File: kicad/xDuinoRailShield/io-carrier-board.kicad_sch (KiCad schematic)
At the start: 6 parts, among them J5 Screw_Terminal_01x02

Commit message: More options, more Partnumbers
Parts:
- J5: LCSC (none) -> C8269
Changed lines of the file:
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@@
         )
         (path "/e63e39d7-6ac0-4ffd-8aa3-1841a4541b55/73623b68-3f11-49c2-b33b-f7aef9e34c5f"
-          (reference "#PWR01") (unit 1)
+          (reference "#PWR0501") (unit 1)
         )
       )
@@
         )
         (path "/e63e39d7-6ac0-4ffd-8aa3-1841a4541b55/73623b68-3f11-49c2-b33b-f7aef9e34c5f"
-          (reference "D1") (unit 1)
+          (reference "D501") (unit 1)
         )
       )
@@
         )
         (path "/e63e39d7-6ac0-4ffd-8aa3-1841a4541b55/73623b68-3f11-49c2-b33b-f7aef9e34c5f"
-          (reference "R1") (unit 1)
+          (reference "R501") (unit 1)
         )
       )
@@
         )
         (path "/e63e39d7-6ac0-4ffd-8aa3-1841a4541b55/73623b68-3f11-49c2-b33b-f7aef9e34c5f"
-          (reference "A1") (unit 1)
+          (reference "A501") (unit 1)
         )
       )
@@
         )
         (path "/e63e39d7-6ac0-4ffd-8aa3-1841a4541b55/73623b68-3f11-49c2-b33b-f7aef9e34c5f"
-          (reference "#PWR09") (unit 1)
+          (reference "#PWR0504") (unit 1)
         )
       )
@@
         )
         (path "/e63e39d7-6ac0-4ffd-8aa3-1841a4541b55/73623b68-3f11-49c2-b33b-f7aef9e34c5f"
-          (reference "R2") (unit 1)
+          (reference "R502") (unit 1)
         )
       )
@@
         )
         (path "/e63e39d7-6ac0-4ffd-8aa3-1841a4541b55/73623b68-3f11-49c2-b33b-f7aef9e34c5f"
+          (reference "#PWR0502") (unit 1)
+        )
+      )
+    )
+  )
+  (symbol (lib_id "Connector:Screw_Terminal_01x02") (at 72.39 59.69 180) (unit 1)
+    (in_bom yes) (on_board yes) (dnp no)
+    (property "Reference" "J5" (at 72.39 62.23 0)
+      (effects (font (size 1.27 1.27)) (justify left))
+    )
+    (property "Value" "Screw_Terminal_01x02" (at 91.44 64.77 0)
+      (effects (font (size 1.27 1.27)) (justify left))
+    )
+    (property "Footprint" "TerminalBlock_4Ucon:TerminalBlock_4Ucon_1x02_P3.50mm_Vertical" (at 72.39 59.69 0)
+      (effects (font (size 1.27 1.27)) hide)
+    )
+    (property "Datasheet" "~" (at 72.39 59.69 0)
+      (effects (font (size 1.27 1.27)) hide)
+    )
+    (property "LCSC" "C8269" (at 72.39 59.69 0)
+      (effects (font (size 1.27 1.27)) hide)
+    )
+    (pin "1")
+    (pin "2")
+    (instances
+      (project "xDuinoRailShield"
+        (path "/e63e39d7-6ac0-4ffd-8aa3-1841a4541b55"
+          (reference "J5") (unit 1)
+        )
+        (path "/e63e39d7-6ac0-4ffd-8aa3-1841a4541b55/73623b68-3f11-49c2-b33b-f7aef9e34c5f"
+          (reference "J501") (unit 1)
+        )
+      )
+    )
+  )
+  (symbol (lib_id "power:+3V3") (at 212.09 52.07 0) (mirror y) (unit 1)
+    (in_bom yes) (on_board yes) (dnp no)
+    (property "Reference" "#PWR03" (at 212.09 55.88 0)
+      (effects (font (size 1.27 1.27)) hide)
+    )
+    (property "Value" "+3.3V" (at 211.709 49.022 90)
+      (effects (font (size 1.27 1.27)) (justify left))
+    )
+    (property "Footprint" "" (at 212.09 52.07 0)
+      (effects (font (size 1.27 1.27)))
+    )
+    (property "Datasheet" "" (at 212.09 52.07 0)
+      (effects (font (size 1.27 1.27)))
+    )
+    (pin "1")
+    (instances
+      (project "xDuinoRailShield"
+        (path "/e63e39d7-6ac0-4ffd-8aa3-1841a4541b55"
           (reference "#PWR03") (unit 1)
         )
-      )
-    )
-  )
-  (symbol (lib_id "Connector:Screw_Terminal_01x02") (at 72.39 59.69 180) (unit 1)
-    (in_bom yes) (on_board yes) (dnp no)
-    (property "Reference" "J5" (at 72.39 62.23 0)
-      (effects (font (size 1.27 1.27)) (justify left))
-    )
-    (property "Value" "Screw_Terminal_01x02" (at 91.44 64.77 0)
-      (effects (font (size 1.27 1.27)) (justify left))
-    )
-    (property "Footprint" "TerminalBlock_4Ucon:TerminalBlock_4Ucon_1x02_P3.50mm_Vertical" (at 72.39 59.69 0)
-      (effects (font (size 1.27 1.27)) hide)
-    )
-    (property "Datasheet" "~" (at 72.39 59.69 0)
-      (effects (font (size 1.27 1.27)) hide)
-    )
-    (property "LCSC" "" (at 72.39 59.69 0)
-      (effects (font (size 1.27 1.27)) hide)
-    )
-    (pin "1")
-    (pin "2")
-    (instances
-      (project "xDuinoRailShield"
-        (path "/e63e39d7-6ac0-4ffd-8aa3-1841a4541b55"
-          (reference "J5") (unit 1)
-        )
-        (path "/e63e39d7-6ac0-4ffd-8aa3-1841a4541b55/73623b68-3f11-49c2-b33b-f7aef9e34c5f"
-          (reference "J1") (unit 1)
-        )
-      )
-    )
-  )
-  (symbol (lib_id "power:+3V3") (at 212.09 52.07 0) (mirror y) (unit 1)
-    (in_bom yes) (on_board yes) (dnp no)
-    (property "Reference" "#PWR03" (at 212.09 55.88 0)
-      (effects (font (size 1.27 1.27)) hide)
-    )
-    (property "Value" "+3.3V" (at 211.709 49.022 90)
-      (effects (font (size 1.27 1.27)) (justify left))
-    )
-    (property "Footprint" "" (at 212.09 52.07 0)
-      (effects (font (size 1.27 1.27)))
-    )
-    (property "Datasheet" "" (at 212.09 52.07 0)
-      (effects (font (size 1.27 1.27)))
-    )
-    (pin "1")
-    (instances
-      (project "xDuinoRailShield"
-        (path "/e63e39d7-6ac0-4ffd-8aa3-1841a4541b55"
-          (reference "#PWR03") (unit 1)
-        )
-        (path "/e63e39d7-6ac0-4ffd-8aa3-1841a4541b55/73623b68-3f11-49c2-b33b-f7aef9e34c5f"
-          (reference "#PWR08") (unit 1)
+        (path "/e63e39d7-6ac0-4ffd-8aa3-1841a4541b55/73623b68-3f11-49c2-b33b-f7aef9e34c5f"
+          (reference "#PWR0503") (unit 1)
         )
       )
@@
         )
         (path "/e63e39d7-6ac0-4ffd-8aa3-1841a4541b55/73623b68-3f11-49c2-b33b-f7aef9e34c5f"
-          (reference "D3") (unit 1)
-        )
-      )
+          (reference "D502") (unit 1)
+        )
+      )

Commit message: Another iteration on the layout
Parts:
- J501: renamed from J5; footprint TerminalBlock_4Ucon:TerminalBlock_4Ucon_1x02_P3.50mm_Vertical -> TerminalBlock:TerminalBlock_bornier-2_P5.08mm
- renumbered A1 to A501, D1 to D501, D3 to D502, R1 to R501, R2 to R502

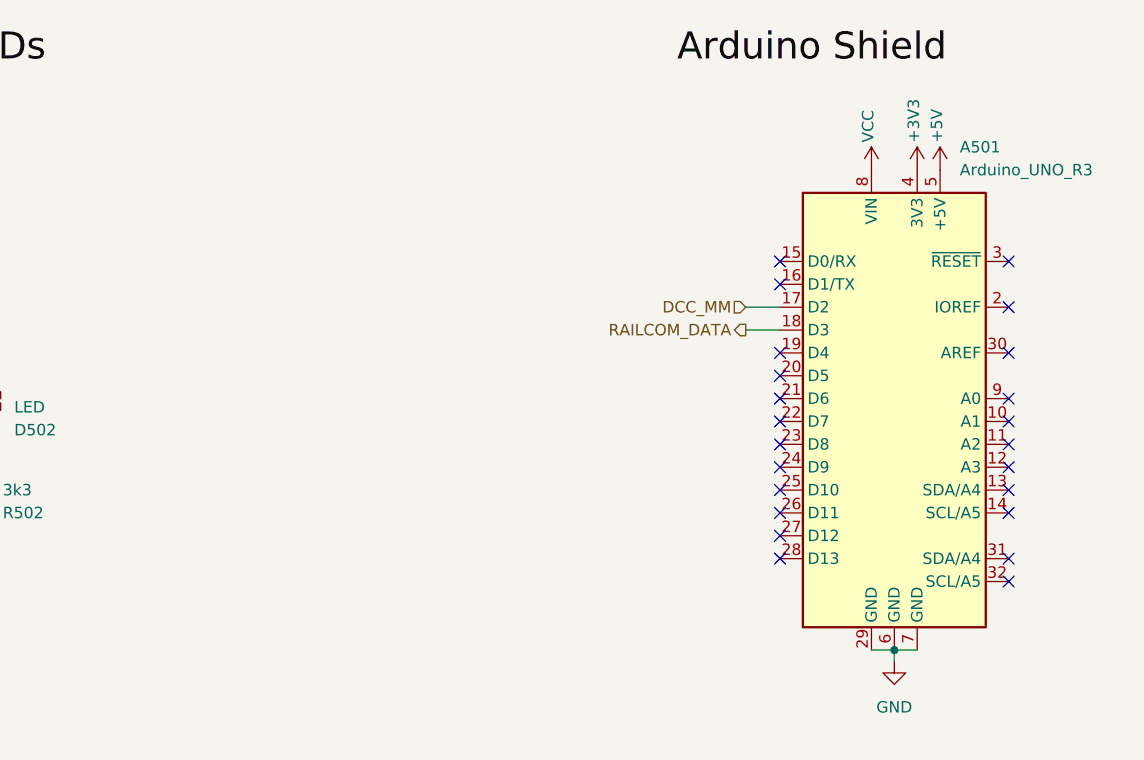
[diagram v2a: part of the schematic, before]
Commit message: Power Rails added to Arduino IO board
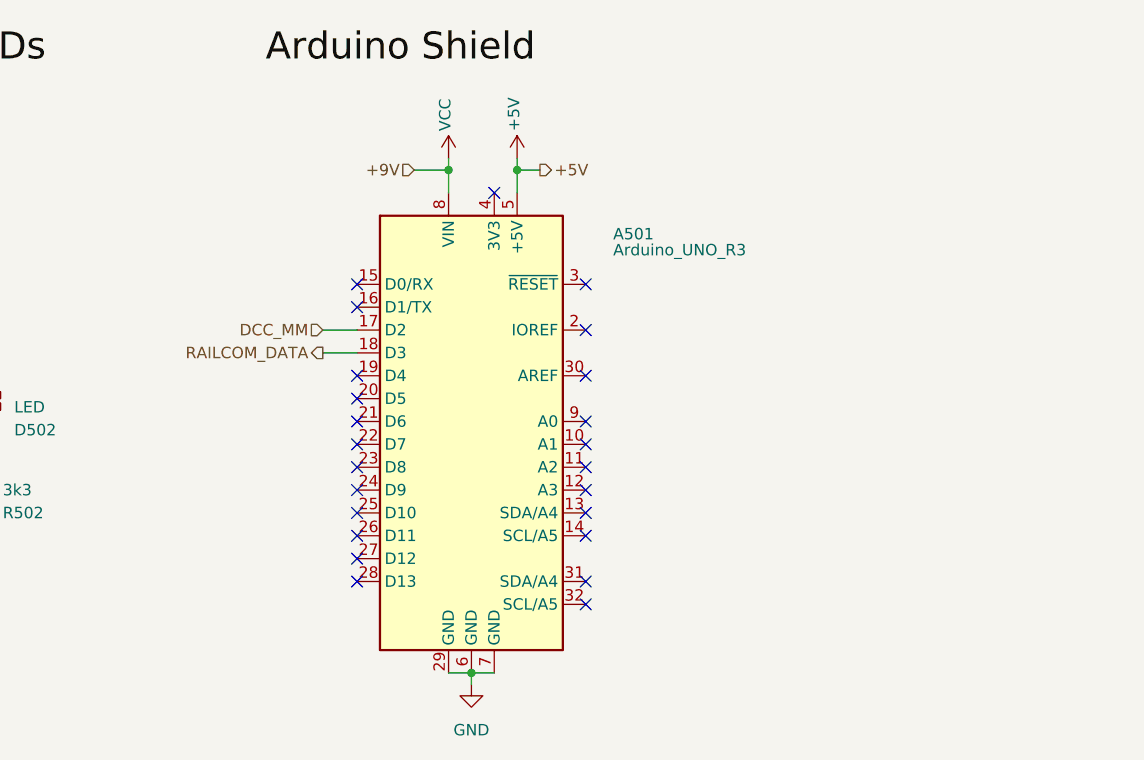
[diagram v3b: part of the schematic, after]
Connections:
- net +3V3: no longer names the net of A501.4 (3V3)
- no-connect marks 23 -> 24
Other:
- moved on the sheet: A501

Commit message: Add Analog signal extraction draft
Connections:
- net ANALOG_5V: now reaches A501.12 (A3)
- no-connect marks 24 -> 23
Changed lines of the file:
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@@
+	)
+	(junction
+		(at 162.56 110.49)
+		(diameter 0)
+		(color 0 0 0 0)
 	)
 	(junction
@@
 	)
 	(no_connect
-		(at 175.26 87.63)
-	)
-	(no_connect
 		(at 175.26 69.85)
 	)
@@
 	(wire
 		(pts
+			(xy 167.64 110.49) (xy 162.56 110.49)
+		)
+		(stroke
+			(width 0)
+			(type default)
+		)
+	)
+	(wire
+		(pts
 			(xy 160.02 50.8) (xy 160.02 52.07)
 		)
@@
 	(wire
 		(pts
-			(xy 162.56 109.22) (xy 162.56 107.95)
+			(xy 162.56 110.49) (xy 162.56 107.95)
+		)
+		(stroke
+			(width 0)
+			(type default)
+		)
+	)
+	(wire
+		(pts
+			(xy 162.56 111.76) (xy 162.56 110.49)
 		)
 		(stroke
@@
 		(pts
 			(xy 160.02 107.95) (xy 162.56 107.95)
+		)
+		(stroke
+			(width 0)
+			(type default)
+		)
+	)
+	(wire
+		(pts
+			(xy 175.26 87.63) (xy 184.15 87.63)
 		)
 		(stroke
@@
 		)
 	)
+	(hierarchical_label "GND"
+		(shape bidirectional)
+		(at 167.64 110.49 0)
+		(fields_autoplaced yes)
+		(effects
+			(font
+				(size 1.27 1.27)
+			)
+			(justify left)
+		)
+	)
 	(hierarchical_label "DCC_MM"
 		(shape input)
@@
 			)
 			(justify right)
+		)
+	)
+	(hierarchical_label "ANALOG_5V"
+		(shape input)
+		(at 184.15 87.63 0)
+		(fields_autoplaced yes)
+		(effects
+			(font
+				(size 1.27 1.27)
+			)
+			(justify left)
 		)
 	)
@@
 	(symbol
 		(lib_id "power:GND")
-		(at 162.56 109.22 0)
+		(at 162.56 111.76 0)
 		(unit 1)
 		(exclude_from_sim no)
@@
 		(fields_autoplaced yes)
 		(property "Reference" "#PWR05"
-			(at 162.56 115.57 0)
+			(at 162.56 118.11 0)
 			(effects
 				(font
@@
 		)
 		(property "Value" "GND"
-			(at 162.56 114.3 0)
+			(at 162.56 116.84 0)
 			(effects
 				(font
@@
 		)
 		(property "Footprint" ""
-			(at 162.56 109.22 0)
+			(at 162.56 111.76 0)
 			(effects
 				(font
@@
 		)
 		(property "Datasheet" ""
-			(at 162.56 109.22 0)
+			(at 162.56 111.76 0)
 			(effects
 				(font
@@
 		)
 		(property "Description" ""
-			(at 162.56 109.22 0)
-			(effects
-				(font
+			(at 162.56 111.76 0)
+			(effects
+				(font

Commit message: xXiaoCentralMini
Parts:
- added JP1: DAC_OUTPUT_SELECT, Jumper:SolderJumper-3_P1.3mm_Bridged12_RoundedPad1.0x1.5mm, symbol Jumper:SolderJumper_3_Bridged12
- added U7: MOUDLE-SEEEDUINO-XIAO-ESP32C3, MOUDLE14P-SMD-2.54-21X17.8MM, symbol MOUDLE-SEEEDUINO-XIAO-ESP32C3:MOUDLE-SEEEDUINO-XIAO-ESP32C3
- A1: renamed from A501; footprint Olis_Footprints:Arduino_UNO_R3_Double_Rows -> Module:Arduino_UNO_R3
- D8: renamed from D501; now not fitted
- D9: renamed from D502; now not fitted
- R12: renamed from R501; footprint Resistor_SMD:R_0805_2012Metric_Pad1.20x1.40mm_HandSolder -> Resistor_SMD:R_0603_1608Metric_Pad0.98x0.95mm_HandSolder; now not fitted
- R13: renamed from R502; footprint Resistor_SMD:R_0805_2012Metric_Pad1.20x1.40mm_HandSolder -> Resistor_SMD:R_0603_1608Metric_Pad0.98x0.95mm_HandSolder; now not fitted
- renumbered J501 to J1
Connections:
- net DAC_NUCLEO: now reaches A1.11 (A2)
- net DAC_NUCLEO: now also JP1.3 (B)
- net DAC_ADAFRUIT_SPARKFUN: now reaches A1.9 (A0)
- net DAC_ADAFRUIT_SPARKFUN: now also JP1.1 (A)
- new net DAC: JP1.2 (C)
- no-connect marks 23 -> 21
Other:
- company: (none) -> Olivier Châtelain
- title: (none) -> xDuinoDecoderDev
- moved on the sheet: A1, J1

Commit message: More nice changes
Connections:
- net AUX1: now reaches A1.21 (D6)
- net AUX2: now reaches A1.22 (D7)
- net AUX3: now reaches A1.23 (D8)
- net AUX4: now reaches A1.24 (D9)
- net AUX5: now reaches A1.25 (D10)
- net AUX6: now reaches A1.26 (D11)
- net AUX7: now reaches A1.27 (D12)
- net AUX8: now reaches A1.28 (D13)
- net DCC_0 renamed DCC0
- net DCC_1 renamed DCC1
- no-connect marks 21 -> 13
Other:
- moved on the sheet: A1, D8, D9, J1, JP1, R12, R13, U7

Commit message: More busses added
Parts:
- renumbered A1 to A601, D8 to D601, D9 to D602, J1 to J601, JP1 to JP601, R12 to R601, R13 to R602, U7 to U601
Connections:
- net AUX5 renamed MOTOR0
- net AUX6 renamed MOTOR1
- net AUX7 renamed F0.FOREWARD
- net AUX8 renamed F0.BACKWARD
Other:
- moved on the sheet: A601, D601, D602, J601, JP601, R601, R602, U601

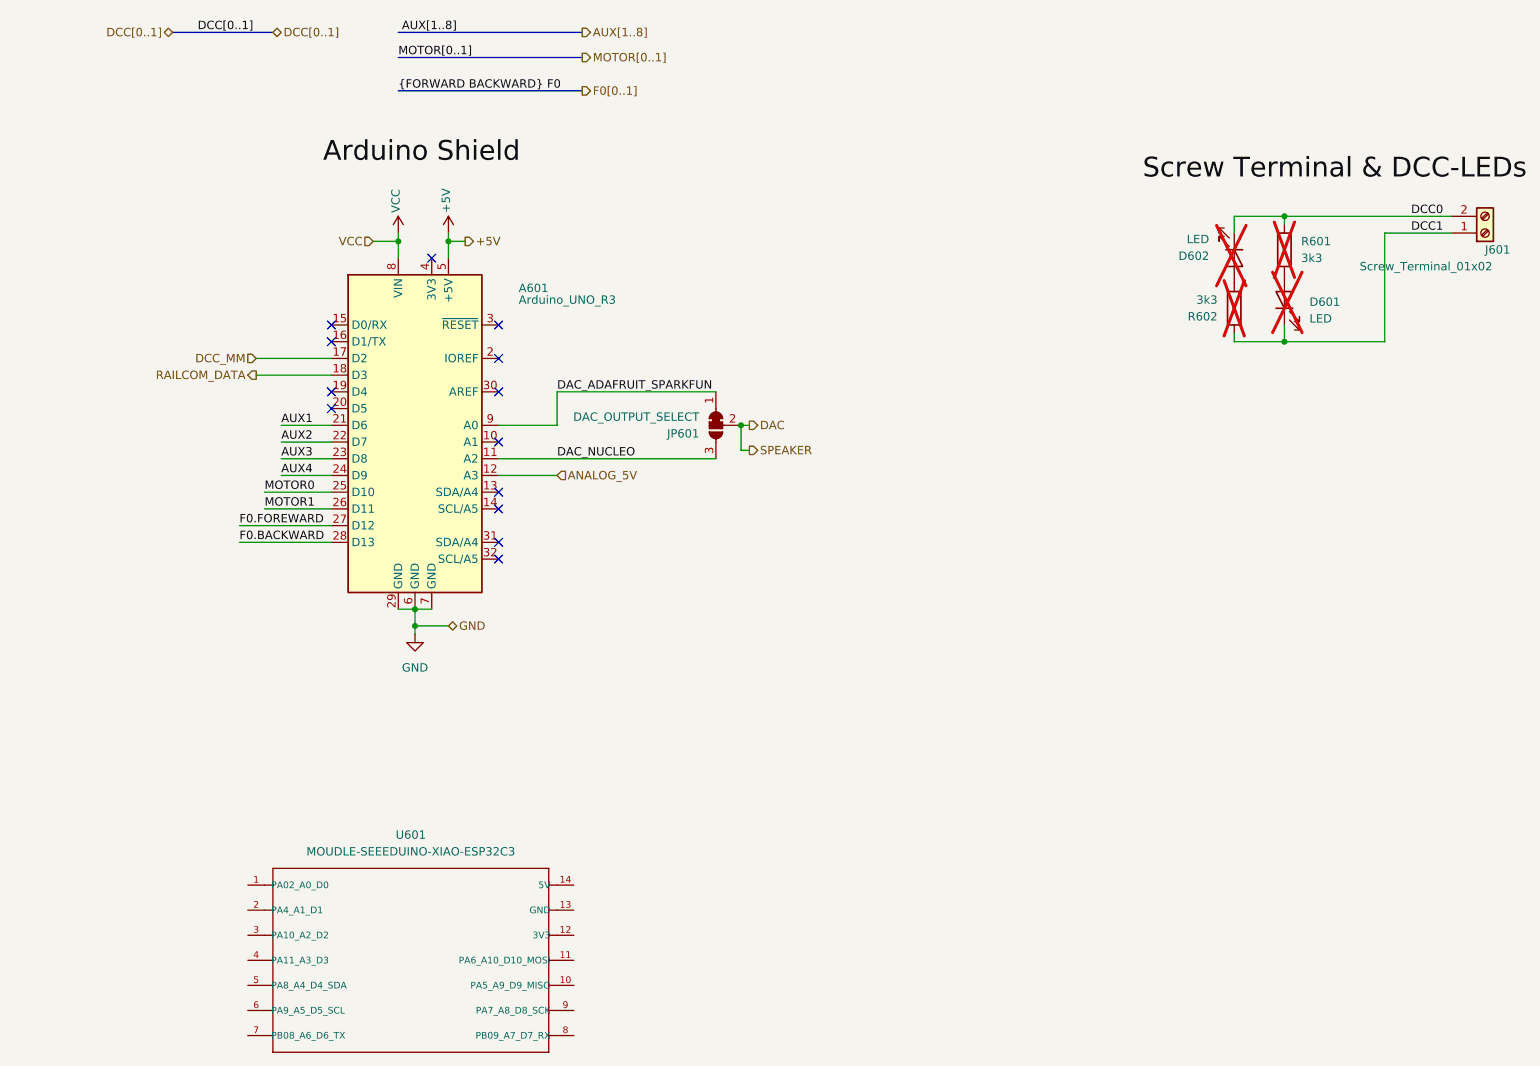
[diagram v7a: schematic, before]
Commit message: Draft of loco decoder
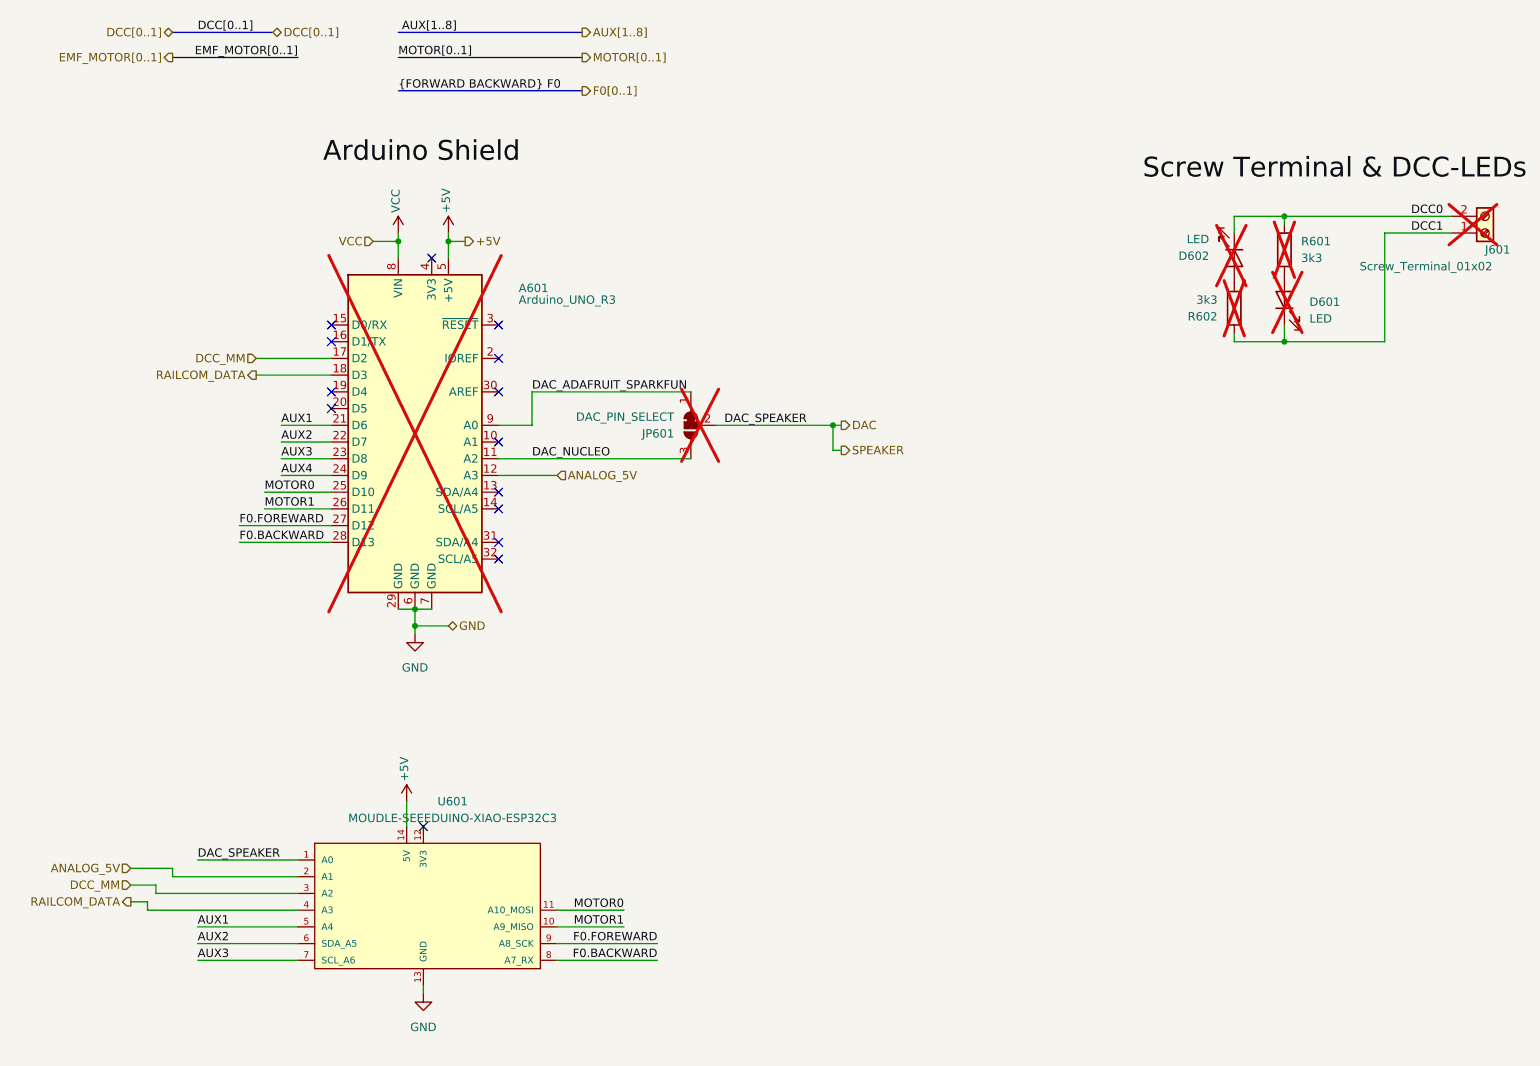
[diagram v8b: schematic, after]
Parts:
- A601, J601: now not fitted; now left out of the parts list
- D601, D602, R601, R602: now left out of the parts list
- JP601: value DAC_OUTPUT_SELECT -> DAC_PIN_SELECT; now not fitted; now left out of the parts list
- U601: footprint MOUDLE14P-SMD-2.54-21X17.8MM -> xiao ESP32C3_PCB:MOUDLE14P-SMD-2.54-21X17.8MM
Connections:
- net +5V: now also U601.14 (5V)
- net ANALOG_5V: now also U601.2 (A1)
- net AUX1: now also U601.5 (A4)
- net AUX2: now also U601.6 (SDA_A5)
- net AUX3: now also U601.7 (SCL_A6)
- net DAC: now also U601.1 (A0)
- net DCC_MM: now also U601.3 (A2)
- net F0.BACKWARD: now also U601.8 (A7_RX)
- net F0.FOREWARD: now also U601.9 (A8_SCK)
- net GND: now also U601.13 (GND)
- net MOTOR0: now also U601.11 (A10_MOSI)
- net MOTOR1: now also U601.10 (A9_MISO)
- net RAILCOM_DATA: now also U601.4 (A3)
- no-connect marks 13 -> 14
